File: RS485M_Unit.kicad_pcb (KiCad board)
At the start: 2 copper layers, 20.6 x 28 mm, 30 parts, among them CN1 CON_GROVE, J1 Conn_01x04, SW1 SW_Push, U1 WB485E, U2 TD1466A, U4 MCU_STC8G1Kxx-8P

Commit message: update readme
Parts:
- removed SW1: SW_Push, Button_Switch_SMD:SW_Push_SPST_NO_Alps_SKRK
- D2: footprint Diode_SMD:D_SOD-123F -> Diode_SMD:D_SOD-323F
- JP6, JP7: value Jumper_2_Open -> Jumper_2_Bridged; footprint Jumper:SolderJumper-2_P1.3mm_Open_Pad1.0x1.5mm -> Jumper:SolderJumper-2_P1.3mm_Bridged_Pad1.0x1.5mm
- R5, R6: moved to F.Cu
- moved D3 22.2 mm to (4.15, 26.5), turned to -90 degrees
- moved R3 15.9 mm to (4.15, 23.4), turned to 90 degrees
- moved R4 13.5 mm to (19.1, 3.83), turned to 90 degrees
- moved JP5 13.4 mm to (18.6, 3.80), turned to 90 degrees
- moved R7 9.25 mm to (18.3, 13.2), turned to -90 degrees
- moved R9 8.76 mm to (19.9, 6.80), turned to -90 degrees
- moved R5 8.71 mm to (0.80, 4.83), turned to -90 degrees
- moved R6 8.08 mm to (0.80, 7.80), turned to 90 degrees
- moved JP6 7.49 mm to (1.30, 4.55), turned to -90 degrees
- moved JP7 6.37 mm to (1.30, 7.85), turned to 90 degrees
- moved R8 6.22 mm to (19.8, 13.2)
- moved C3 4.63 mm to (13.9, 15.2)
- moved U2 3.11 mm to (19.0, 9.90)
- moved D2 1.75 mm to (16.5, 10.1), turned to 90 degrees
- moved R10 1.65 mm to (2.65, 23.4), turned to -90 degrees
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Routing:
- net +5V: track 70.1 -> 55.4 mm
- net /SW: track 14.7 -> 0.00 mm
- net GND: track 66.0 -> 79.9 mm, vias 6 -> 5
- net /BUS_B: track 15.0 -> 28.1 mm
- net Net-(JP9-A): track 21.7 -> 9.44 mm, vias 3 -> 4
- net /BUS_A: track 20.3 -> 31.1 mm
- net Net-(U2-EN): track 10.9 -> 1.07 mm, vias 2 -> 0
- net /TX_EN: track 42.8 -> 33.9 mm, vias 4 -> 2
- net Net-(U2-FB): track 10.0 -> 2.90 mm, vias 2 -> 0
- net Net-(U2-BST): track 1.48 -> 3.07 mm, vias 0 -> 2
- net Net-(JP6-B): track 1.78 -> 0.47 mm, vias 0 -> 1
- net Net-(JP7-B): track 1.78 -> 0.52 mm, vias 0 -> 1
- net Net-(JP5-A): track 1.49 -> 0.31 mm
- net /RXD: track 22.1 -> 21.0 mm, vias 2 -> 0
- net Net-(D2-K): track 5.35 -> 6.23 mm
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
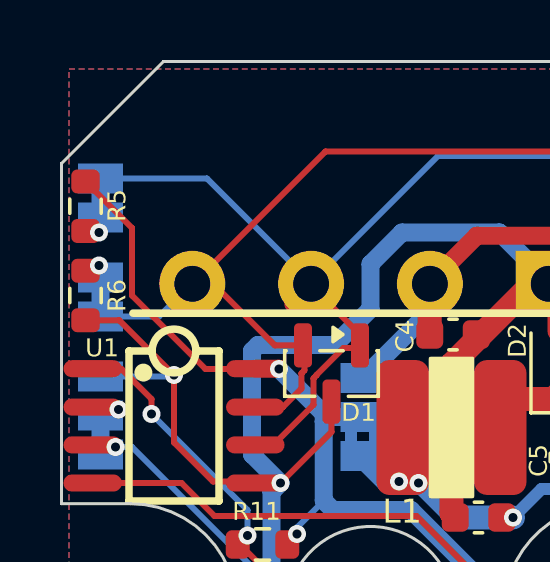
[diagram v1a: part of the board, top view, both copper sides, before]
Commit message: add photo, JP6/7 modify
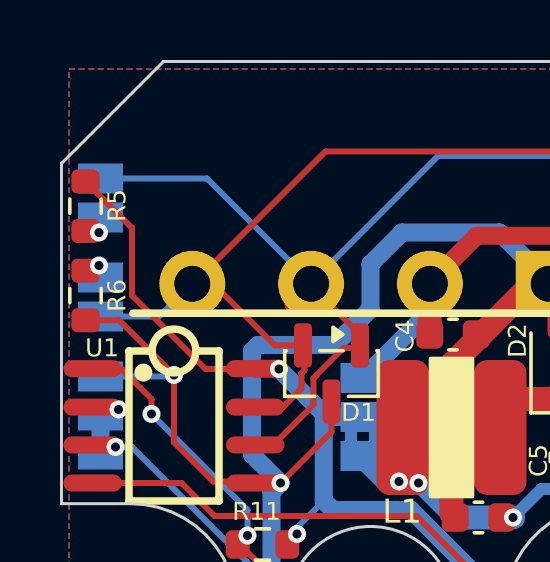
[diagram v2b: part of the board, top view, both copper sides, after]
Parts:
- JP6, JP7: value Jumper_2_Bridged -> Jumper_2_Open; footprint Jumper:SolderJumper-2_P1.3mm_Bridged_Pad1.0x1.5mm -> Jumper:SolderJumper-2_P1.3mm_Open_Pad1.0x1.5mm
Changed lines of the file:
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@@
 			)
 		)
-		(property "LCSC" "C190475"
+		(property "LCSC" ""
 			(at 0 0 90)
 			(unlocked yes)
@@
 		(embedded_fonts no)
 	)
-	(footprint "Jumper:SolderJumper-2_P1.3mm_Bridged_Pad1.0x1.5mm"
+	(footprint "Jumper:SolderJumper-2_P1.3mm_Open_Pad1.0x1.5mm"
 		(layer "B.Cu")
 		(at 1.3 7.85 90)
-		(descr "SMD Solder Jumper, 1x1.5mm Pads, 0.3mm gap, bridged with 1 copper strip")
-		(tags "net tie solder jumper bridged")
+		(descr "SMD Solder Jumper, 1x1.5mm Pads, 0.3mm gap, open")
+		(tags "solder jumper open")
 		(property "Reference" "JP7"
-			(at 0.1 1.7 90)
+			(at 0 1.8 270)
 			(layer "B.SilkS")
 			(effects
@@
 			)
 		)
-		(property "Value" "Jumper_2_Bridged"
-			(at 0 -1.9 90)
+		(property "Value" "Jumper_2_Open"
+			(at 0 -1.9 270)
 			(layer "B.Fab")
 			(effects
@@
 			)
 		)
-		(property "Description" "Jumper, 2-pole, closed/bridged"
+		(property "Description" "Jumper, 2-pole, open"
 			(at 0 0 270)
 			(unlocked yes)
@@
 		(zone_connect 1)
 		(attr exclude_from_pos_files allow_soldermask_bridges)
-		(net_tie_pad_groups "1, 2")
-		(fp_poly
-			(pts
-				(xy -0.25 0.3) (xy 0.25 0.3) (xy 0.25 -0.3) (xy -0.25 -0.3)
-			)
-			(stroke
-				(width 0)
-				(type solid)
-			)
-			(fill yes)
-			(layer "B.Cu")
-		)
 		(fp_rect
 			(start -0.15 0.75)
@@
 		(embedded_fonts no)
 	)
-	(footprint "Jumper:SolderJumper-2_P1.3mm_Bridged_Pad1.0x1.5mm"
+	(footprint "Jumper:SolderJumper-2_P1.3mm_Open_Pad1.0x1.5mm"
 		(layer "B.Cu")
 		(at 1.3 4.55 -90)
-		(descr "SMD Solder Jumper, 1x1.5mm Pads, 0.3mm gap, bridged with 1 copper strip")
-		(tags "net tie solder jumper bridged")
+		(descr "SMD Solder Jumper, 1x1.5mm Pads, 0.3mm gap, open")
+		(tags "solder jumper open")
 		(property "Reference" "JP6"
-			(at -0.05 -1.7 270)
+			(at -0.05 -1.7 90)
 			(layer "B.SilkS")
 			(effects
@@
 			)
 		)
-		(property "Value" "Jumper_2_Bridged"
+		(property "Value" "Jumper_2_Open"
 			(at 0 -1.9 90)
 			(layer "B.Fab")
@@
 			)
 		)
-		(property "Description" "Jumper, 2-pole, closed/bridged"
+		(property "Description" "Jumper, 2-pole, open"
 			(at 0 0 90)
 			(unlocked yes)
@@
 		(zone_connect 1)
 		(attr exclude_from_pos_files allow_soldermask_bridges)
-		(net_tie_pad_groups "1, 2")
-		(fp_poly
-			(pts
-				(xy -0.25 0.3) (xy 0.25 0.3) (xy 0.25 -0.3) (xy -0.25 -0.3)
-			)
-			(stroke
-				(width 0)
-				(type solid)
-			)
-			(fill yes)
-			(layer "B.Cu")
-		)
 		(fp_rect
 			(start -0.15 0.75)
